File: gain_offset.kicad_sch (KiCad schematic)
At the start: 34 parts, among them U3 AD8337BCPZ-REEL-ND, U4 LMH6551MA, U5 AD8337BCPZ-REEL-ND, U7 LMH6551MA

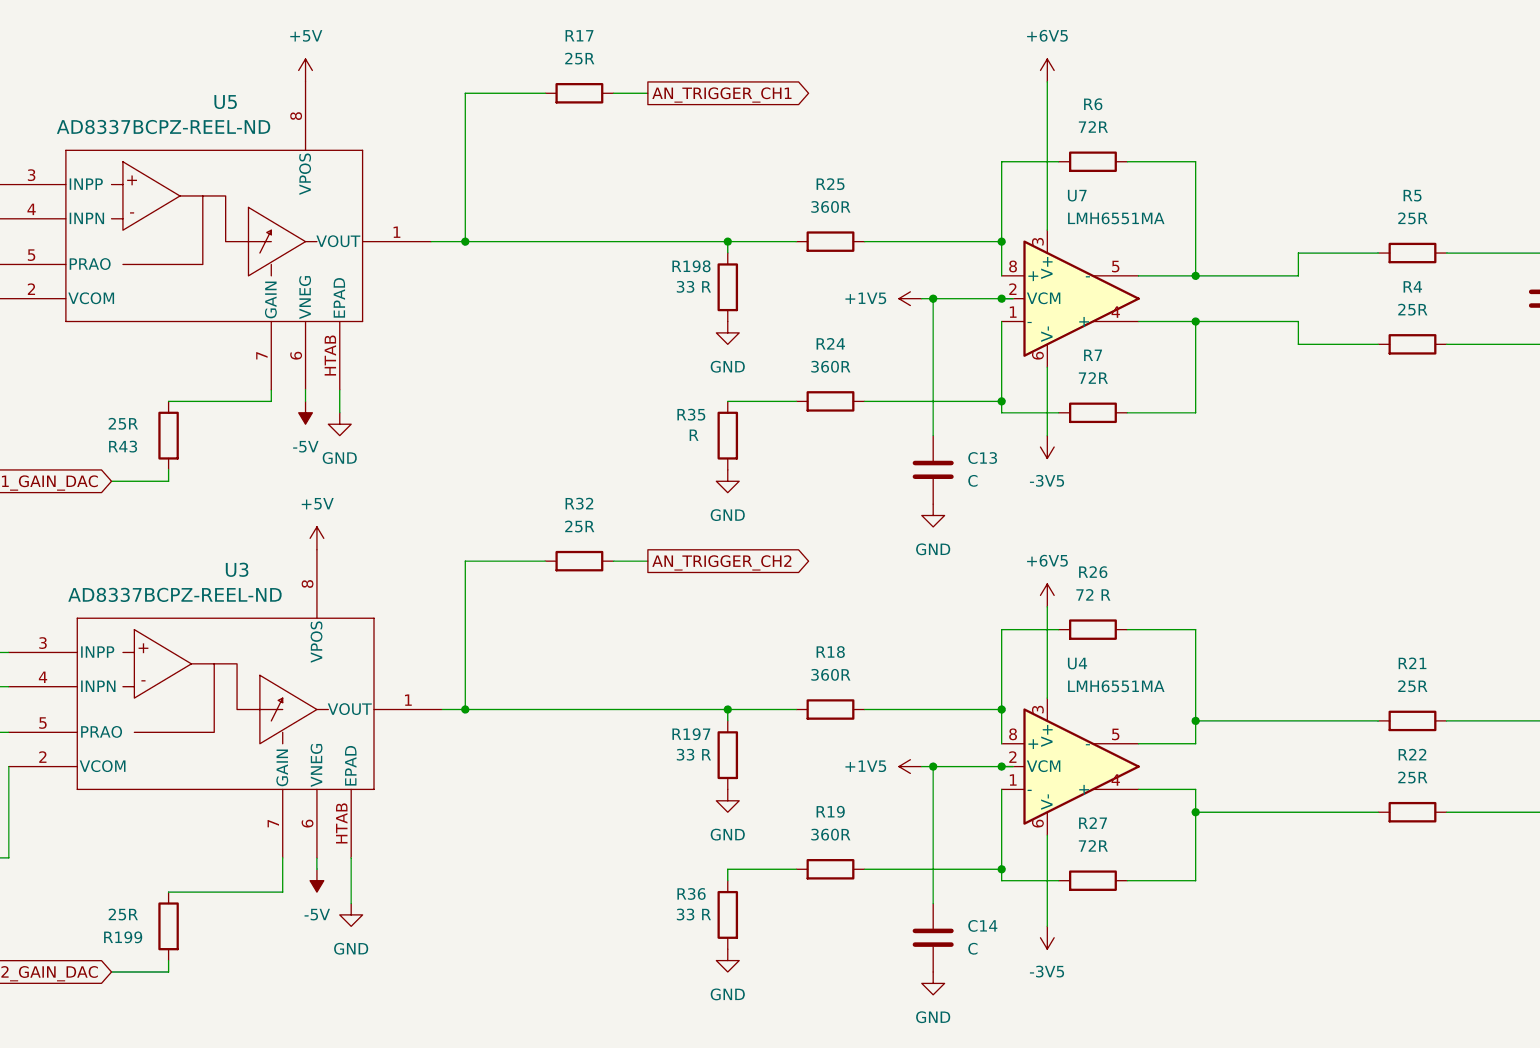
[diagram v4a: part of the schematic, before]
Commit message: Mostly finished schematics, without decoupling and power
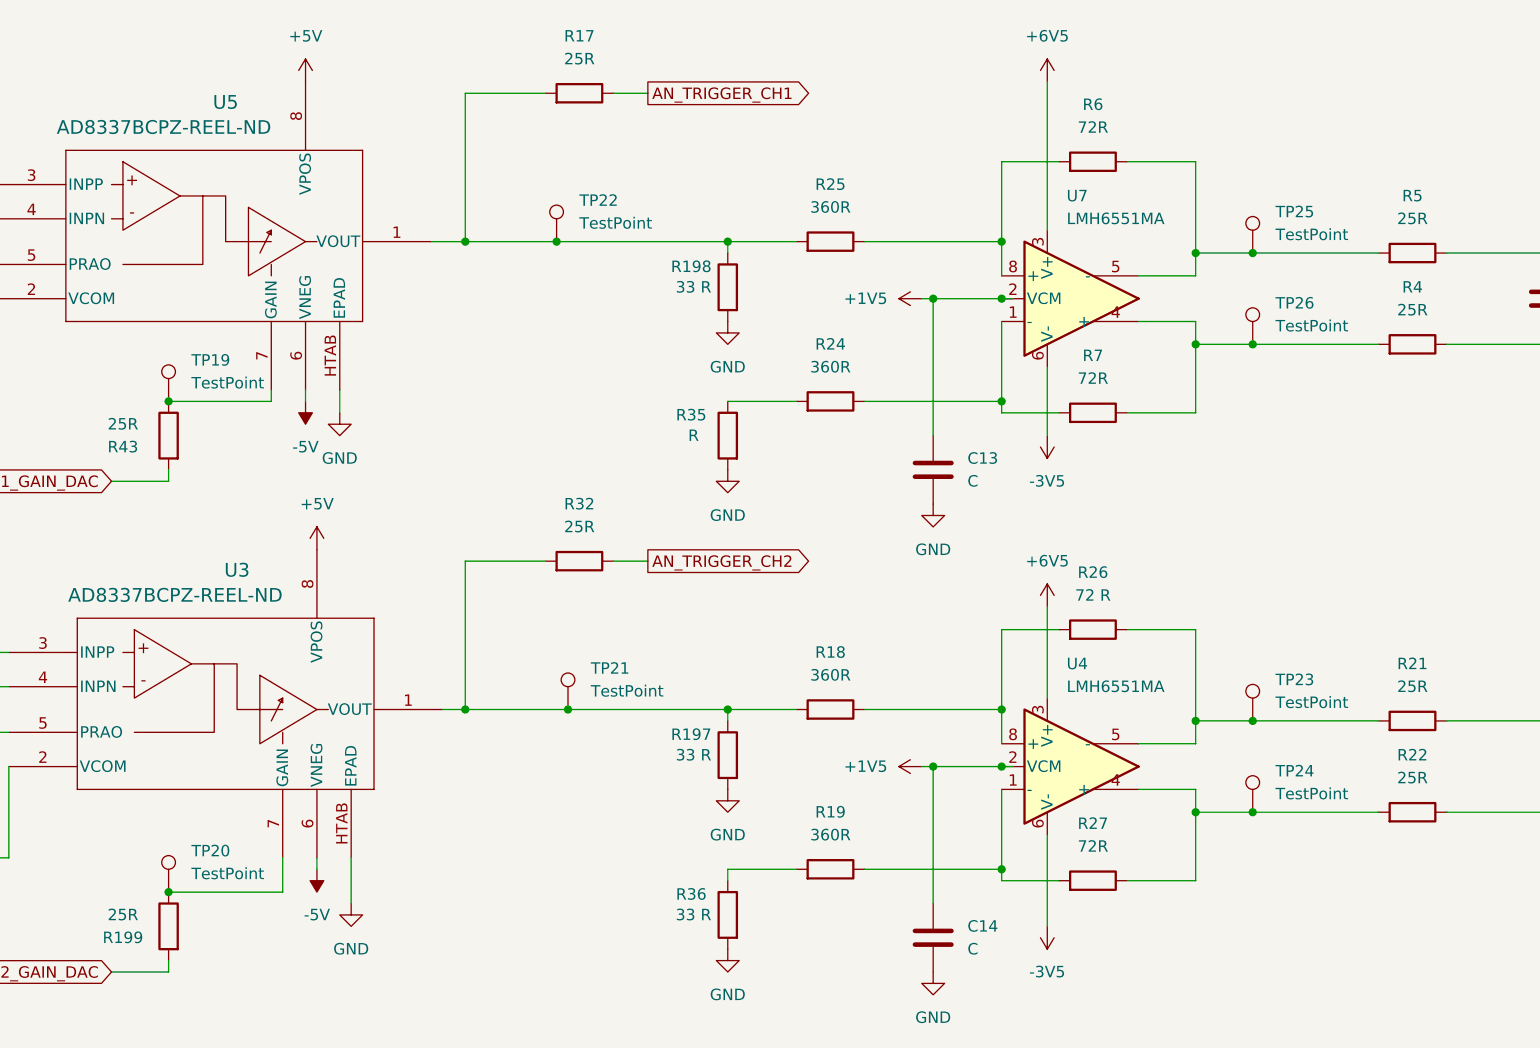
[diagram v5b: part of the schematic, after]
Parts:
- added TP19, TP20, TP21, TP22, TP23, TP24, TP25, TP26: TestPoint, Connector_PinHeader_2.54mm:PinHeader_1x01_P2.54mm_Vertical, symbol Connector:TestPoint
- C11, C12: footprint Capacitor_SMD:C_0603_1608Metric_Pad1.08x0.95mm_HandSolder -> (none)
- R17, R199, R21, R22, R32, R4, R43, R5: footprint Resistor_SMD:R_0402_1005Metric_Pad0.72x0.64mm_HandSolder -> Resistor_SMD:R_1206_3216Metric
- R18, R19, R197, R198, R200, R24, R25, R26, R27, R28, R29, R30, R31, R35, R36, R44, R6, R7: footprint (none) -> Resistor_SMD:R_1206_3216Metric
- U3, U5: footprint CP_8_2_ADI -> footprints:CP_8_2_ADI
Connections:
- net at R17.2, R198.1, R25.2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: now also TP22.1
- net at R43.1, U5.7 (GAIN): now also TP19.1
- net at R22.2, R27.1, U4.4 (+): now also TP24.1
- net at R5.2, R6.1, U7.5 (-): now also TP25.1
- net at R18.2, R197.1, R32.2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: now also TP21.1
- net at R21.2, R26.1, U4.5 (-): now also TP23.1
- net at R4.2, R7.1, U7.4 (+): now also TP26.1
- net at R199.1, U3.7 (GAIN): now also TP20.1

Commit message: Finished schematic?
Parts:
- added C72, C75, C79, C82, C85, C90, C91, C96: 100nF, symbol Device:C
- added C73, C76, C80, C83, C86, C89, C92, C95: 1uF, symbol Device:C
- added C74, C77, C81, C84, C87, C88, C93, C94: 10uF, symbol Device:C
- added L19, L21, L23, L25, L27, L30, L31, L34: LCBB-601, symbol Device:L
- added L20, L22, L24, L26, L28, L29, L32, L33: 0.68uH, 0.8Ohm, symbol Device:L
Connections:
- net +5V: now also L28.1, L29.1; no longer U3.8 (VPOS), U5.8 (VPOS)
- net +6V5: now also L20.1, L24.1; no longer U4.3 (V+), U7.3 (V+)
- net -3V5: now also L22.1, L26.1; no longer U4.6 (V-), U7.6 (V-)
- net -5V: now also L32.1, L33.1; no longer U3.6 (VNEG), U5.6 (VNEG)
- net GND: now also C72.2, C73.1, C74.1, C75.2, C76.1, C77.1, C79.2, C80.1, C81.1, C82.2, C83.1, C84.1, C85.2, C86.1, C87.1, C88.1, C89.1, C90.2, C91.2, C92.1, C93.1, C94.1, C95.1, C96.2
- new net: C91.1, C92.2, C93.2, L31.2, U5.6 (VNEG)
- new net: C85.1, C86.2, C87.2, L27.2, U5.8 (VPOS)
- new net: C75.1, C76.2, C77.2, L21.2, U7.6 (V-)
- new net: C79.1, C80.2, C81.2, L23.2, U4.3 (V+)
- new net: L29.2, L30.1
- new net: C94.2, C95.2, C96.1, L34.2, U3.6 (VNEG)
- new net: C72.1, C73.2, C74.2, L19.2, U7.3 (V+)
- new net: L25.1, L26.2
- new net: L21.1, L22.2
- new net: C88.2, C89.2, C90.1, L30.2, U3.8 (VPOS)
- new net: C82.1, C83.2, C84.2, L25.2, U4.6 (V-)
- new net: L33.2, L34.1
- new net: L27.1, L28.2
- new net: L31.1, L32.2
- new net: L23.1, L24.2
- new net: L19.1, L20.2
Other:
- note removed: "0.2 Gain to convert from +5 -5V to +1V -1V 2Vpp"
- moved on the sheet: C11, C12, C13, C14, R17, R18, R19, R197, R198, R199, R200, R21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
